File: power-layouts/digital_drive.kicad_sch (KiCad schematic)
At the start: 20 parts, among them Q1501 MMBT3904L, Q1502 MMBT3904L, Q1503 MMBT3904L, U1501 EPC23104ENGRT, U1502 EPC23104ENGRT

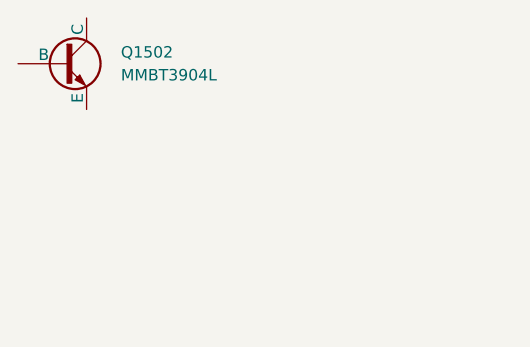
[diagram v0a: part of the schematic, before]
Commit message: changed layout of pcbs to be more distinct
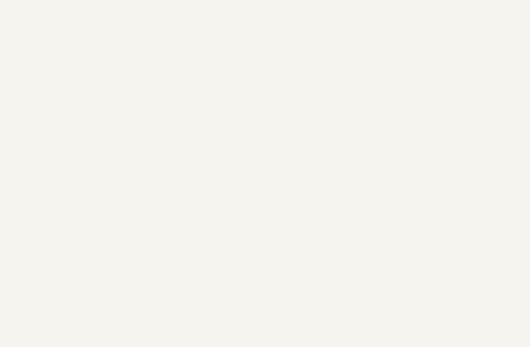
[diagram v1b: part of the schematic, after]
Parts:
- removed Q1502: MMBT3904L, BR_SOT:SOT-23, symbol BR_Transistors:BJT_N_MMBT3904L
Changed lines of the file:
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@@
-		)
-	)
-	(symbol
-		(lib_id "BR_Transistors:BJT_N_MMBT3904L")
-		(at -11818.62 -6525.26 0)
-		(unit 1)
-		(exclude_from_sim no)
-		(in_bom yes)
-		(on_board yes)
-		(dnp no)
-		(fields_autoplaced yes)
-		(property "Reference" "Q1502"
-			(at -11812.27 -6526.5301 0)
-			(effects
-				(font
-					(size 1.27 1.27)
-				)
-				(justify left)
-			)
-		)
-		(property "Value" "MMBT3904L"
-			(at -11812.27 -6523.9901 0)
-			(effects
-				(font
-					(size 1.27 1.27)
-				)
-				(justify left)
-			)
-		)
-		(property "Footprint" "BR_SOT:SOT-23"
-			(at -11818.62 -6601.46 0)
-			(effects
-				(font
-					(size 1.27 1.27)
-				)
-				(justify left)
-				(hide yes)
-			)
-		)
-		(property "Datasheet" "https://www.onsemi.com/pdf/datasheet/mmbt3904lt1-d.pdf"
-			(at -11818.62 -6598.92 0)
-			(effects
-				(font
-					(size 1.27 1.27)
-				)
-				(justify left)
-				(hide yes)
-			)
-		)
-		(property "Description" "NPN BJT 40V 200mA 300mW 300MHz SOT-23-3"
-			(at -11818.62 -6588.76 0)
-			(effects
-				(font
-					(size 1.27 1.27)
-				)
-				(justify left)
-				(hide yes)
-			)
-		)
-		(property "Manufacturer" "onsemi"
-			(at -11818.62 -6596.38 0)
-			(effects
-				(font
-					(size 1.27 1.27)
-				)
-				(justify left)
-				(hide yes)
-			)
-		)
-		(property "Manufacturer Part Num" "MMBT3904LT1G"
-			(at -11818.62 -6593.84 0)
-			(effects
-				(font
-					(size 1.27 1.27)
-				)
-				(justify left)
-				(hide yes)
-			)
-		)
-		(property "BRE Number" "BRE-000400"
-			(at -11818.62 -6591.3 0)
-			(effects
-				(font
-					(size 1.27 1.27)
-				)
-				(justify left)
-				(hide yes)
-			)
-		)
-		(property "Supplier 1" "DigiKey"
-			(at -11818.62 -6586.22 0)
-			(effects
-				(font
-					(size 1.27 1.27)
-				)
-				(justify left)
-				(hide yes)
-			)
-		)
-		(property "Supplier Part Num 1" "MMBT3904LT1GOSCT-ND"
-			(at -11818.62 -6583.68 0)
-			(effects
-				(font
-					(size 1.27 1.27)
-				)
-				(justify left)
-				(hide yes)
-			)
-		)
-		(property "Supplier 2" "DigiKey"
-			(at -11818.62 -6581.14 0)
-			(effects
-				(font
-					(size 1.27 1.27)
-				)
-				(justify left)
-				(hide yes)
-			)
-		)
-		(property "Supplier Part Num 2" "MMBT3904LT1GOSTR-ND"
-			(at -11818.62 -6578.6 0)
-			(effects
-				(font
-					(size 1.27 1.27)
-				)
-				(justify left)
-				(hide yes)
-			)
-		)
-		(property "Supplier 3" "JLCPCB"
-			(at -11818.62 -6576.06 0)
-			(effects
-				(font
-					(size 1.27 1.27)
-				)
-				(justify left)
-				(hide yes)
-			)
-		)
-		(property "Supplier Part Num 3" "C81464/ C84555"
-			(at -11818.62 -6573.52 0)
-			(effects
-				(font
-					(size 1.27 1.27)
-				)
-				(justify left)
-				(hide yes)
-			)
-		)
-		(property "JLCPCB Part Num" "C81464"
-			(at -11818.62 -6565.9 0)
-			(effects
-				(font
-					(size 1.27 1.27)
-				)
-				(justify left)
-				(hide yes)
-			)
-		)
-		(pin "3"
-		)
-		(pin "2"
-		)
-		(pin "1"
-		)
-		(instances
-			(project ""
-				(path "/2a5ce3ef-537a-4122-a1be-ef76186bc0d7/e1c72b00-0544-40b2-bdd8-a4cf7df3ac65/1e5859a0-f8d4-4fa9-a838-2018b8a35fcb"
-					(reference "Q1502")
-					(unit 1)
-				)
-			)
 		)
 	)
